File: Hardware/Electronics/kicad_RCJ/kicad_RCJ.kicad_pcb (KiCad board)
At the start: 2 copper layers, 113 x 151.1 mm, 78 parts, among them J10 Conn_01x04_M1_extra, J11 Conn_01x04_M2_extra, J12 Conn_01x04_M3_extra, J13 Conn_01x04_M4_extra, J14 Conn_01x06_teensy_left_extra, J15 Conn_01x04_teensy_right_extra, J16 Conn_01x07_IO_expander_extra, J17 Conn_02x03_I2C, J18 Conn_02x05_3V3_GND, J19 Conn_02x05_5V_GND, J2 Conn_01x06_IMU_extra, J20 Conn_01x06_BNO085_extra, J21 Conn_01x06_ISM20948_extra, J22 Conn_01x02_LSM5DSOX_LIS3MDL_e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, J23 VBAT_meas_conn, J24 Conn_01x02, J25 Conn_01x02, J26 Conn_01x02, J27 Conn_01x02, J28 Conn_01x02_5V, J29 Conn_01x02_3.3V, J3 Conn_01x02_colsens_interrupt, J4 Conn_01x02_5V, J5 Conn_01x02_3V3, J6 Conn_01x02_I2C1, J7 Conn_01x01_LOP, J8 Conn_01x03_IO_expander_interr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, J9 Conn_01x06_LED, M5 Servo1, M6 Servo2, U1 DRV8874, U12 VL53L0/1X, U13 VL53L0/1X, U14 VL53L0/1X, U15 VL53L0/1X, U16 VL53L0/1X, U17 VL53L0/1X, U18 VL53L0/1X, U2 DRV8874, U20 BNO085, U21 ICM20948, U22 LSM6DSOX+LIS3MDL, U23 TCS34725, U24 APDS9960, U25 VL53L0/1X, U3 DRV8874, U4 DRV8874

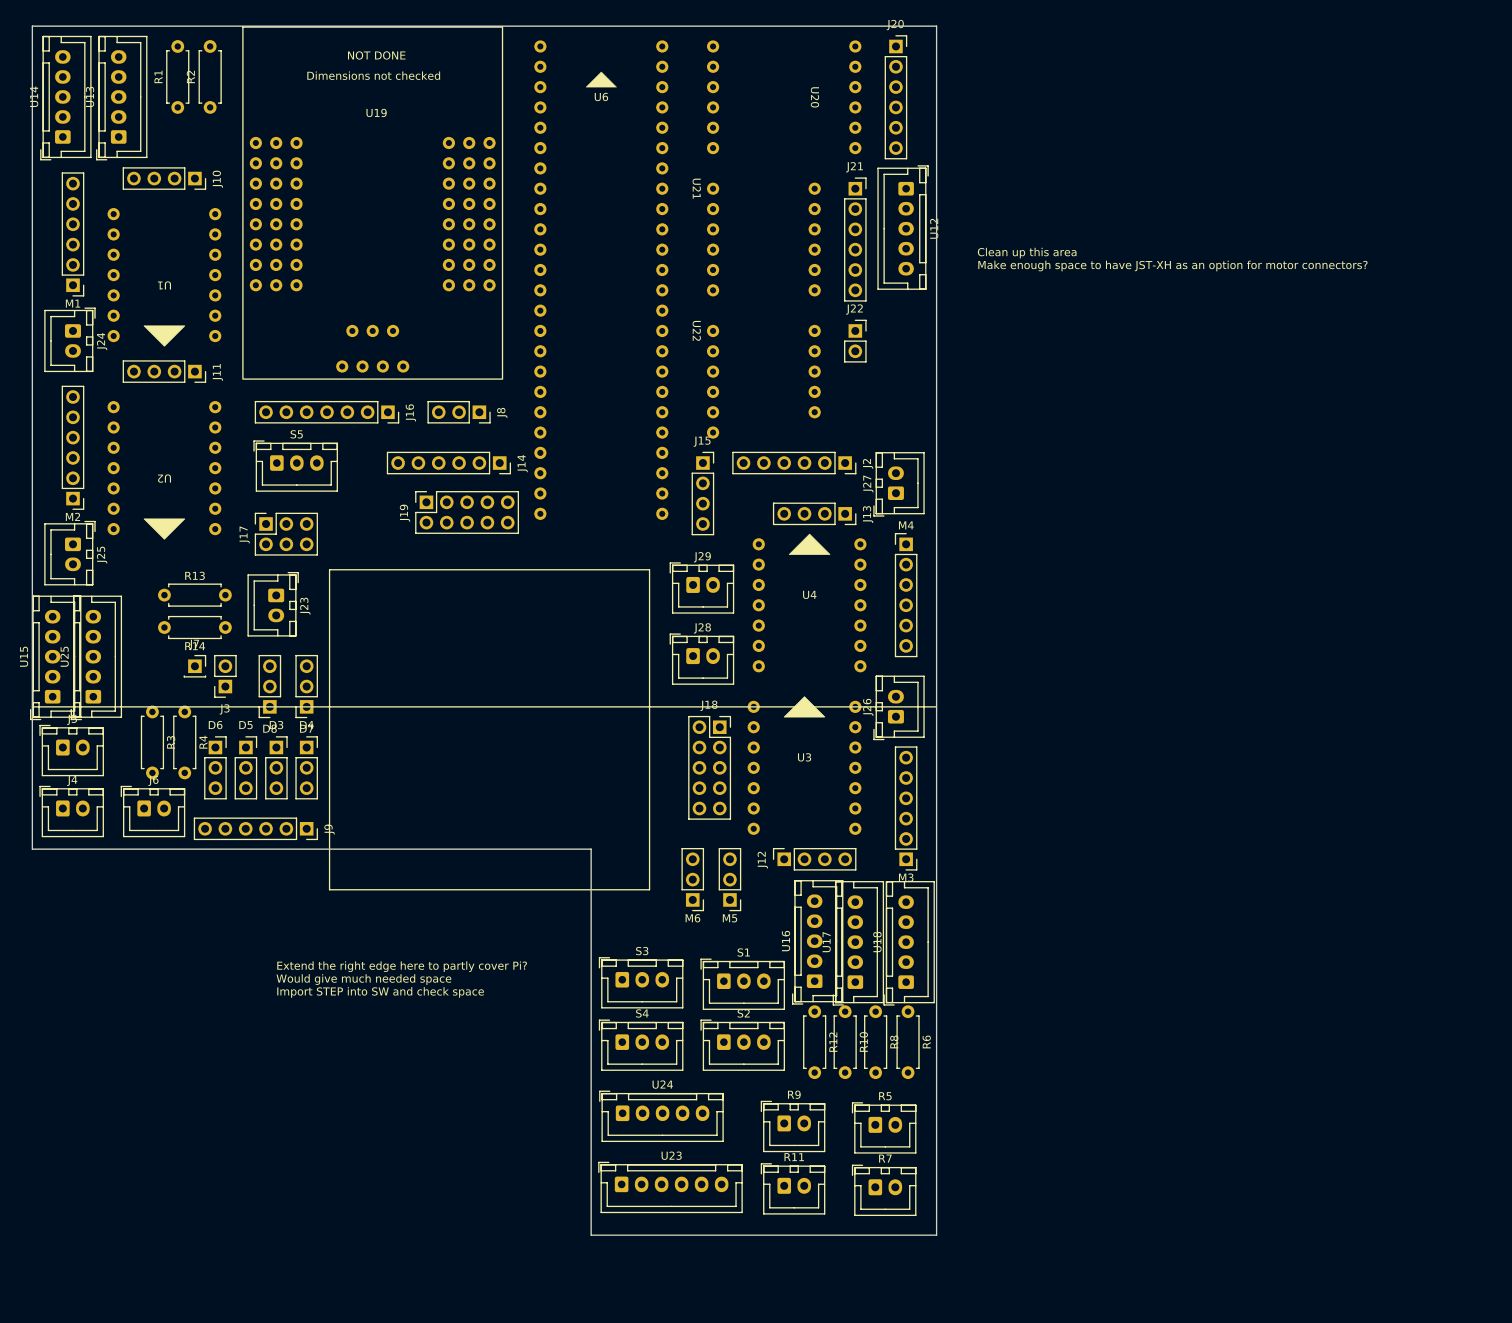
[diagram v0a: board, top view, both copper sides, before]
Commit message: enlarged PCB outline and rearranged
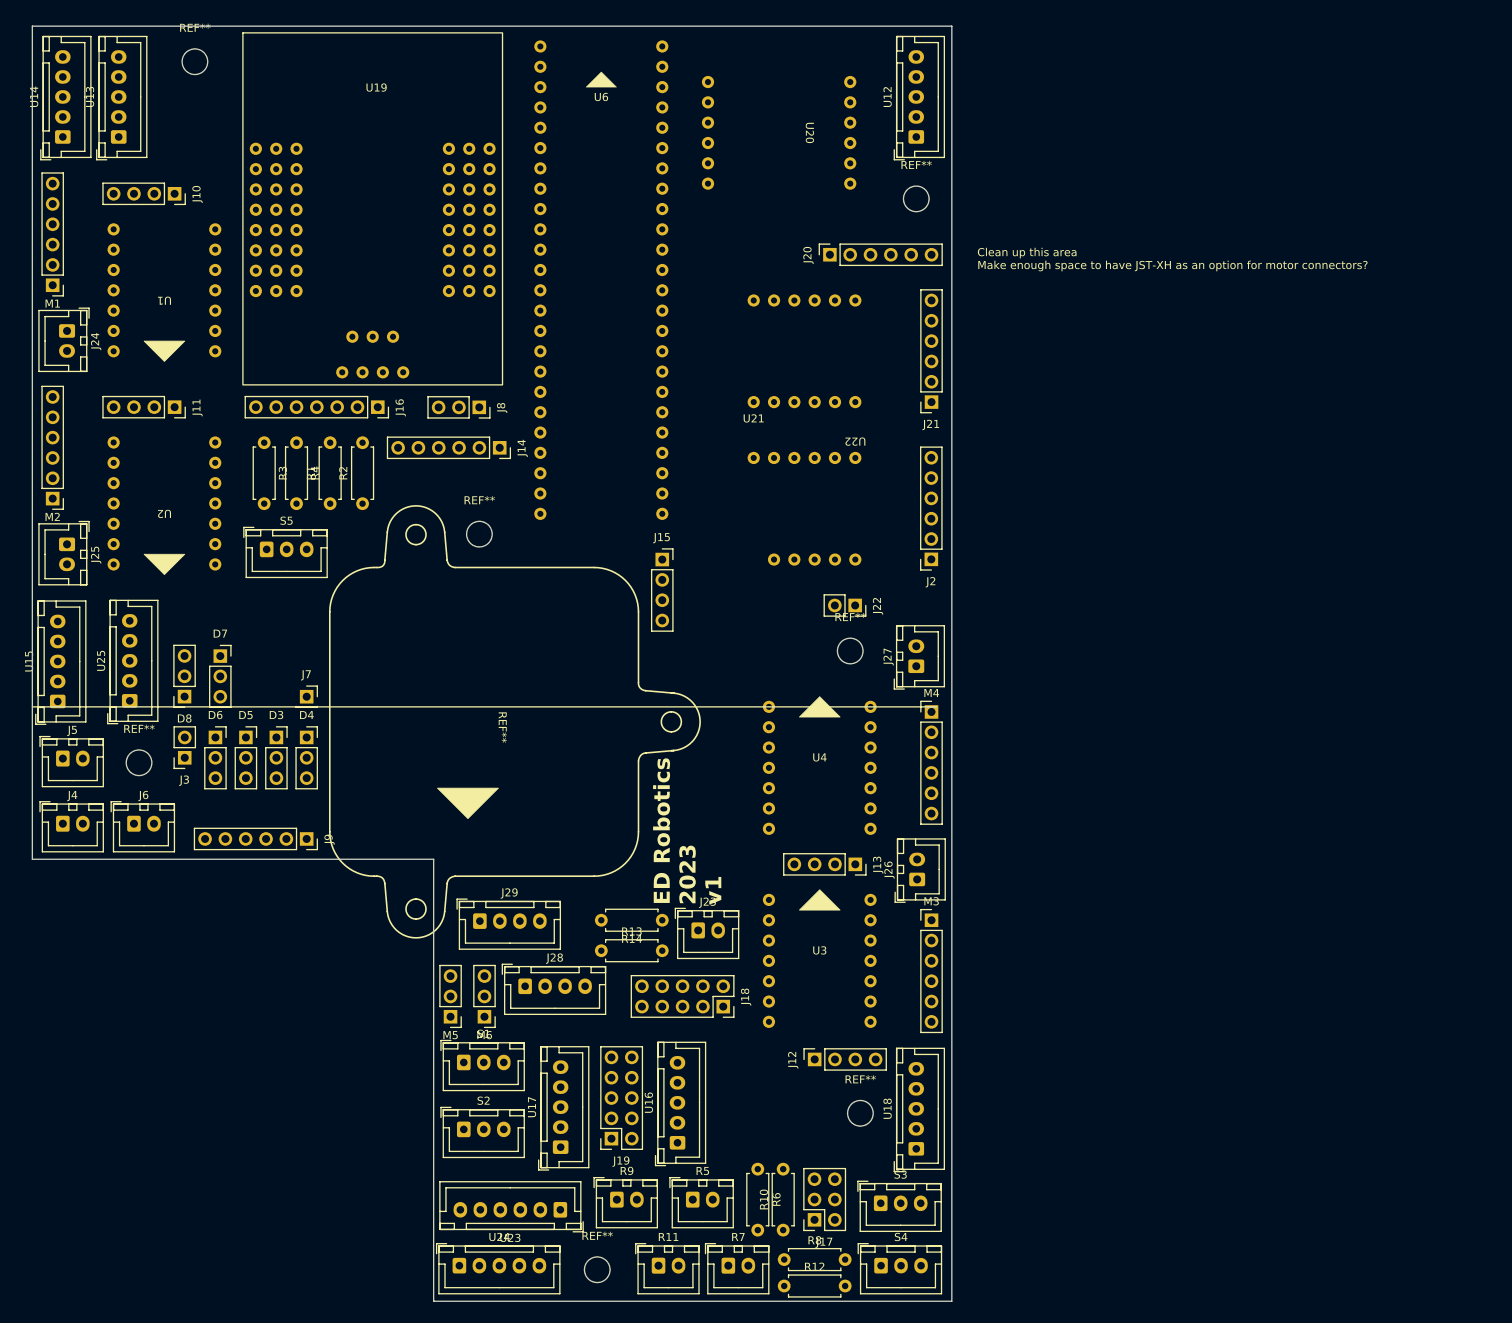
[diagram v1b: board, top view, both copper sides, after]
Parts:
- added REF**: MountingHole_3.2mm_M3, MountingHole:MountingHole_3.2mm_M3, F.Cu at (53.3, 37.5)
- added REF**: MountingHole_3.2mm_M3, MountingHole:MountingHole_3.2mm_M3, F.Cu at (136.5, 168.9)
- added REF**: MountingHole_3.2mm_M3, MountingHole:MountingHole_3.2mm_M3, F.Cu at (143.5, 54.6)
- added REF**: MountingHole_3.2mm_M3, MountingHole:MountingHole_3.2mm_M3, F.Cu at (88.9, 96.5)
- added REF**: MountingHole_3.2mm_M3, MountingHole:MountingHole_3.2mm_M3, F.Cu at (103.6, 188.5)
- added REF**: lidar, RCJ2024_kicad_footprints:lidar, F.Cu at (91.3, 120.7)
- added REF**: MountingHole_3.2mm_M3, MountingHole:MountingHole_3.2mm_M3, F.Cu at (135.3, 111.1)
- added REF**: MountingHole_3.2mm_M3, MountingHole:MountingHole_3.2mm_M3, F.Cu at (46.4, 125.1)
- J28, J29: footprint Connector_JST:JST_XH_B2B-XH-A_1x02_P2.50mm_Vertical -> Connector_JST:JST_XH_B4B-XH-A_1x04_P2.50mm_Vertical
- S5: value ~ -> SW_LOP
- moved J17 110.8 mm to (130.8, 182.2), turned to 180 degrees
- moved J19 82.8 mm to (105.4, 172.1), turned to 180 degrees
- moved R13 70.4 mm to (104.1, 148.6)
- moved J23 67.3 mm to (116.2, 146.1), turned to 0 degrees
- moved R14 65.7 mm to (111.8, 144.8)
- moved R1 53.1 mm to (70.2, 92.7)
- moved R2 53.1 mm to (74.3, 92.7)
- moved J29 49.8 mm to (89.0, 144.9)
- moved J28 46.3 mm to (94.6, 153.0)
- moved J13 43.8 mm to (135.9, 137.8)
- moved S4 42.7 mm to (139.1, 188.0)
- moved S3 42.7 mm to (139.1, 180.2)
- moved U17 42.2 mm to (99.1, 173.1)
- moved M5 37.9 mm to (85.3, 156.8)
- moved R4 36.4 mm to (66.0, 85.1)
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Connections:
- D7 pad 1: +5V -> GND
- D7 pad 3: GND -> +5V
- D8 pad 1: +5V -> GND
- D8 pad 3: GND -> +5V
- J17 pad 1: SDA -> SCL
- J17 pad 3: SDA -> SCL
- J17 pad 4: SCL -> SDA
- J17 pad 6: SCL -> SDA
- J18 pad 1: +3.3V -> GND
- J18 pad 10: GND -> +3.3V
- J18 pad 3: +3.3V -> GND
- J18 pad 5: +3.3V -> GND
- J18 pad 6: GND -> +3.3V
- J18 pad 8: GND -> +3.3V
- J19 pad 1: +5V -> GND
- J19 pad 10: GND -> +5V
- J19 pad 3: +5V -> GND
- J19 pad 5: +5V -> GND
- J19 pad 6: GND -> +5V
- J19 pad 8: GND -> +5V
- J28 pad 2: +5V -> GND
- J29 pad 2: +3.3V -> GND
- J4 pad 1: +3.3V -> GND
- J4 pad 2: GND -> +3.3V
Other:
- board size 113 x 151.1 mm -> 114.9 x 159.4 mm
- board text added: "ED Robotics 2023 v1"
- board text removed: "Extend the right edge here to partly cover Pi? Would give much needed space Import STEP into SW and check space"

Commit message: increased component spacing and fixed custom footprints
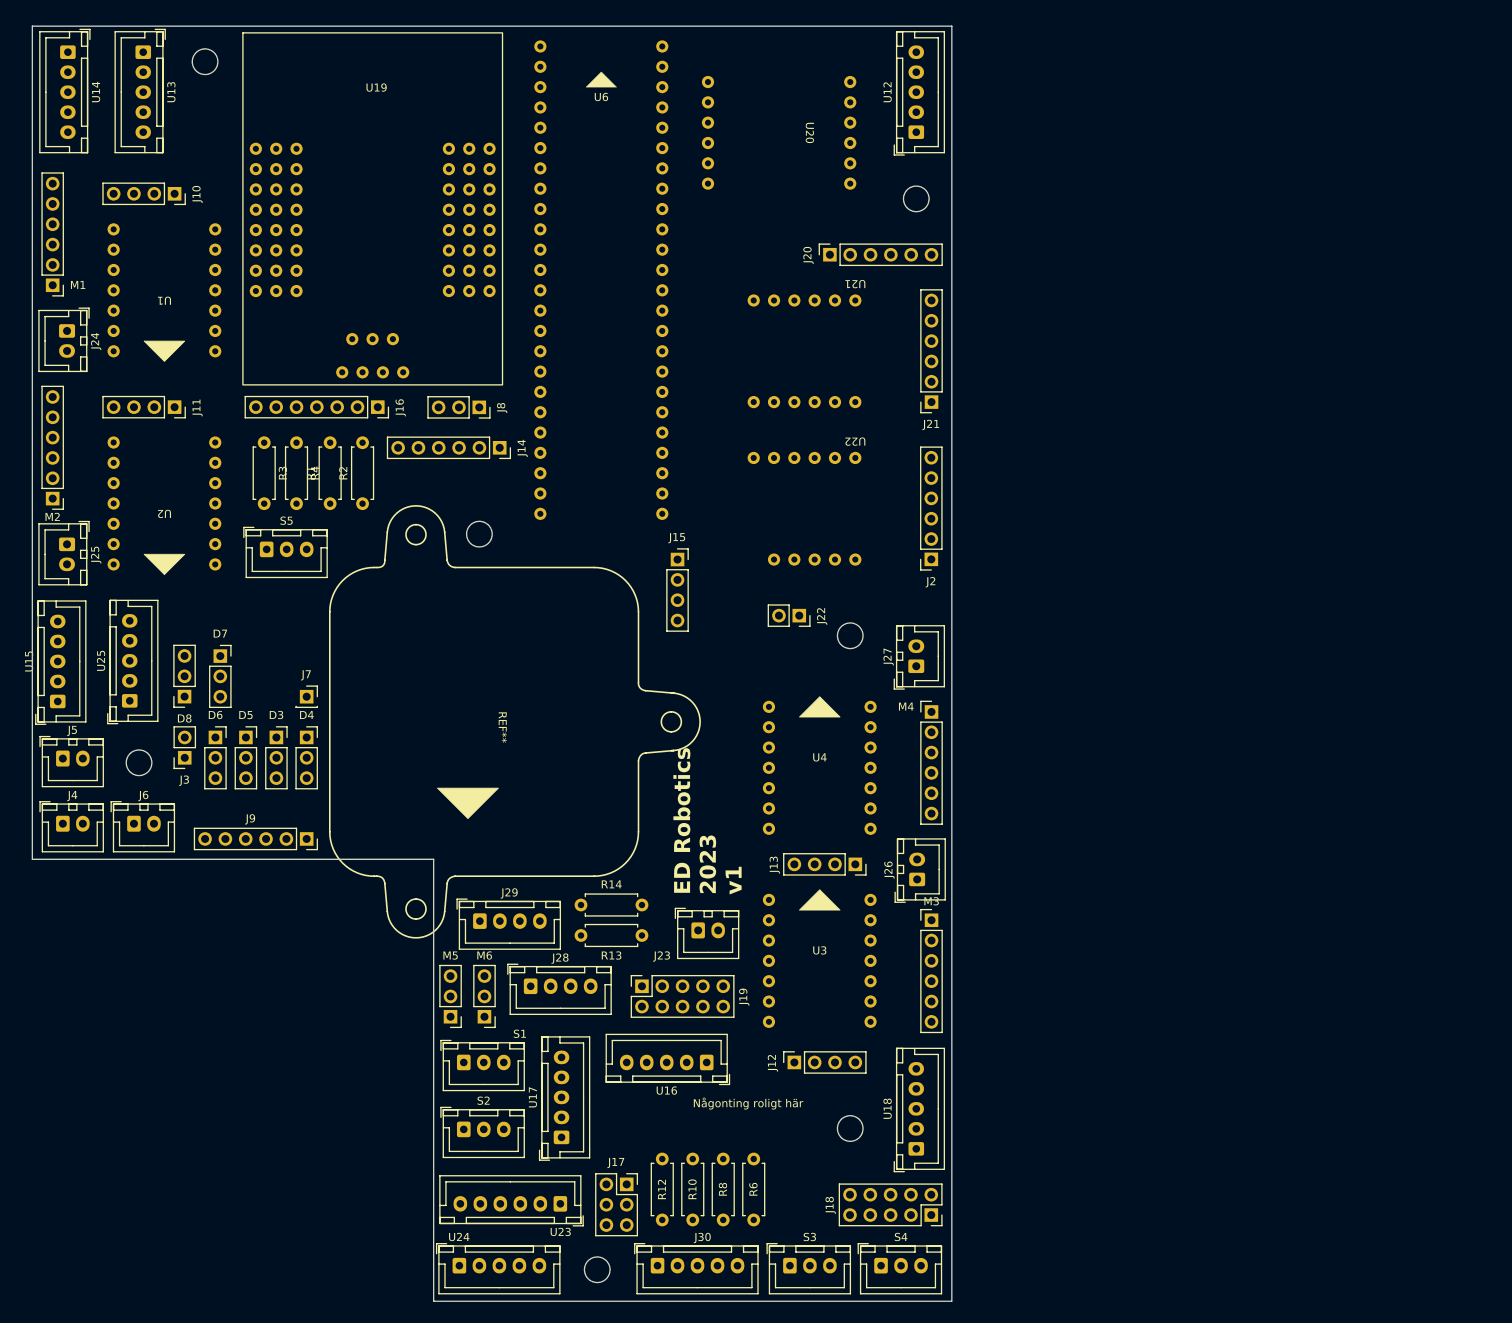
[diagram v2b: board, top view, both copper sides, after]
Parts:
- removed R11, R5, R7, R9: R_Photo, Connector_JST:JST_XH_B2B-XH-A_1x02_P2.50mm_Vertical
- added J30: Conn_01x05_photoresistors, Connector_JST:JST_XH_B5B-XH-A_1x05_P2.50mm_Vertical, F.Cu at (111.2, 188.0)
- moved J18 36.8 mm to (145.4, 181.6)
- moved J17 23.9 mm to (107.3, 177.8), turned to 0 degrees
- moved J19 19.4 mm to (109.2, 153.0), turned to 90 degrees
- moved U21 18.0 mm to (135.9, 67.3), turned to 180 degrees
- moved R12 17.3 mm to (111.8, 182.2), turned to 90 degrees
- moved S3 13.8 mm to (127.7, 188.0)
- moved R10 11.4 mm to (115.6, 182.2)
- moved U13 11.0 mm to (46.9, 36.3), turned to -90 degrees
- moved U16 10.7 mm to (117.3, 162.6), turned to 180 degrees
- moved U14 10.6 mm to (37.5, 36.3), turned to -90 degrees
- moved R8 9.09 mm to (119.4, 182.2), turned to 90 degrees
- moved J22 7.10 mm to (128.9, 106.7)
- moved R6 6.37 mm to (123.2, 182.2), turned to 90 degrees
- moved R13 3.18 mm to (101.6, 146.7)
- moved R14 3.18 mm to (109.2, 142.9)
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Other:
- board text added: "Någonting roligt här"
- board text removed: "Clean up this area Make enough space to have JST-XH as an option for motor connectors?"

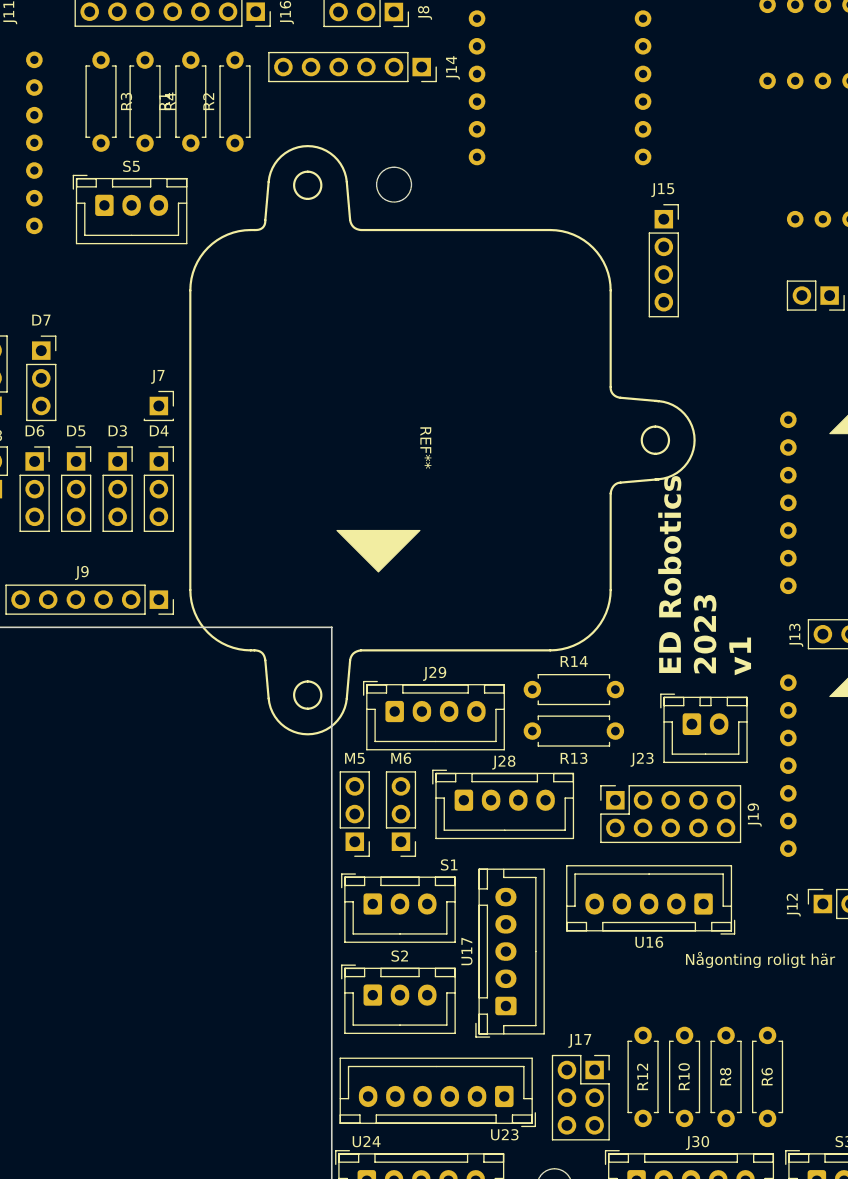
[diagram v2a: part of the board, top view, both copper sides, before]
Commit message: enlarged resistor footprint
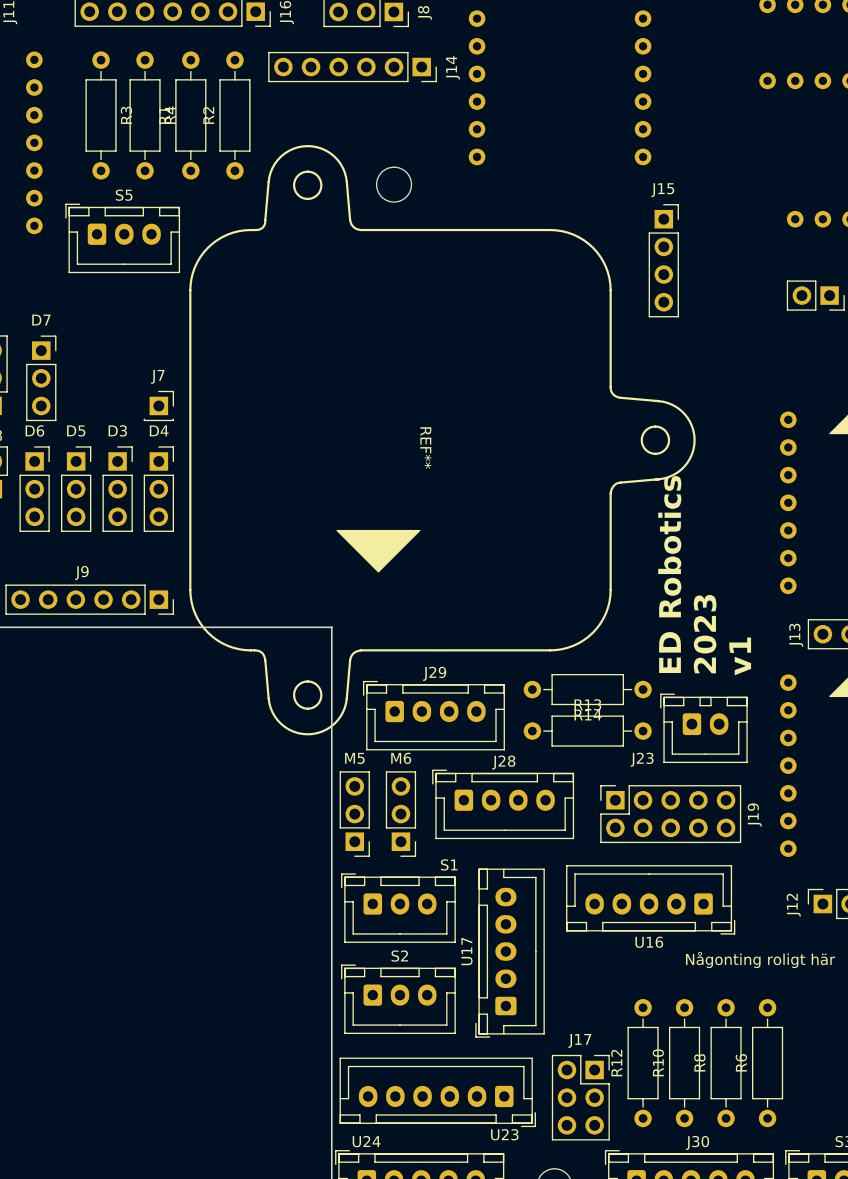
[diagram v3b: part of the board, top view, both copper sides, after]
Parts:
- R1, R10, R12, R13, R14, R2, R3, R4, R6, R8: footprint Resistor_THT:R_Axial_DIN0207_L6.3mm_D2.5mm_P7.62mm_Horizontal -> Resistor_THT:R_Axial_DIN0207_L6.3mm_D2.5mm_P10.16mm_Horizontal
- moved S5 2.73 mm to (61.6, 101.1)
- moved R1 2.54 mm to (70.2, 95.2)
- moved R14 2.54 mm to (111.8, 142.9)
- moved R2 2.54 mm to (74.3, 95.2)

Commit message: did a lot of wiring
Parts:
- moved J18 62.0 mm to (114.9, 127.6), turned to 0 degrees
- moved R13 44.8 mm to (128.9, 182.2)
- moved R14 44.8 mm to (139.1, 178.4)
- moved J23 44.8 mm to (143.5, 181.6), turned to 90 degrees
- moved J20 12.7 mm to (145.4, 61.6), turned to -90 degrees
- moved R12 12.6 mm to (120.7, 173.4), turned to 180 degrees
- moved R2 11.1 mm to (69.8, 85.1), turned to -90 degrees
- moved R1 10.7 mm to (73.7, 85.1), turned to -90 degrees
- moved S1 10.5 mm to (96.4, 167.0), turned to -90 degrees
- moved J19 10.3 mm to (102.2, 145.4)
- moved J13 8.89 mm to (127.0, 137.8), turned to 90 degrees
- moved R10 7.65 mm to (120.7, 176.5), turned to 180 degrees
- moved U16 6.62 mm to (111.9, 166.3), turned to 90 degrees
- moved S5 5.07 mm to (66.0, 103.6), turned to -90 degrees
- moved D7 4.42 mm to (56.5, 116.2), turned to 180 degrees
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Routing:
- net +3.3V: track 0.00 -> 613.6 mm, vias 0 -> 11
- net SCL: track 0.00 -> 272.6 mm, vias 0 -> 17
- net SDA: track 0.00 -> 256.2 mm, vias 0 -> 10
- net Net-(J3-Pin_1): track 0.00 -> 84.6 mm, vias 0 -> 2
- net +5V: track 0.00 -> 75.4 mm, vias 0 -> 1
- net Net-(J3-Pin_2): track 0.00 -> 73.7 mm, vias 0 -> 6
- net SDA1: track 0.00 -> 73.6 mm
- net Net-(U12-XSHUT): track 0.00 -> 73.1 mm
- net SCL1: track 0.00 -> 68.1 mm
- net Net-(M1-ENC_A_OUT): track 0.00 -> 66.5 mm, vias 0 -> 2
- net Net-(M1-ENC_B_OUTPUT): track 0.00 -> 66.0 mm, vias 0 -> 2
- net Net-(J2-Pin_6): track 0.00 -> 57.7 mm, vias 0 -> 2
- net Net-(U19-PA7): track 0.00 -> 47.3 mm, vias 0 -> 6
- net Net-(J2-Pin_5): track 0.00 -> 43.6 mm
- net Net-(S4-NO): track 0.00 -> 42.6 mm
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- added copper zone on B.Cu, net GND
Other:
- outline, holes or cut-outs redrawn
- board text removed: "ED Robotics 2023 v1"
- board text removed: "Någonting roligt här"
